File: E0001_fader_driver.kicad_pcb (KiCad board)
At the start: 4 copper layers, 107 x 17 mm, 53 parts, among them J1 SM04B-GHS-TB, J2 61300611021, U1 STM32C051F6P6, U2 MCP1703AT-3302E/MB, U3 DRV8210PDSGR, U4 TPS259470ARPW

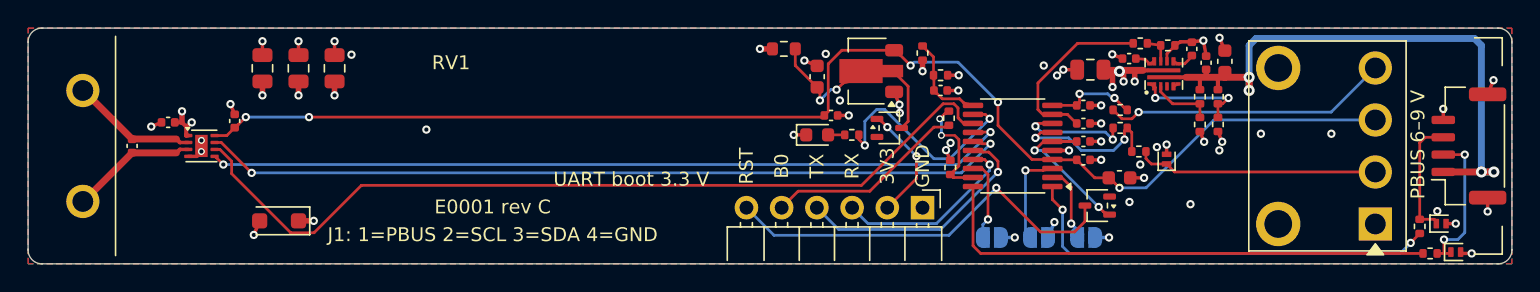
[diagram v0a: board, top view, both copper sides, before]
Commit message: TraceMaker experiment: placed (tracemaker-place routable, U3/U4/RV1 locked, hand intent fixes)
Tracks and vias stripped. RV1 locked. Placement from tracemaker-place
--mode routable on a proxy (RV1 courtyards as footprint keep-outs, F/B
pours removed), then C13, C1, C6, C7, C17 moved next to their IC pins
and silkscreen nudges. Not for fab.

Co-Authored-By: Claude Opus 5.5 <noreply@anthropic.com>
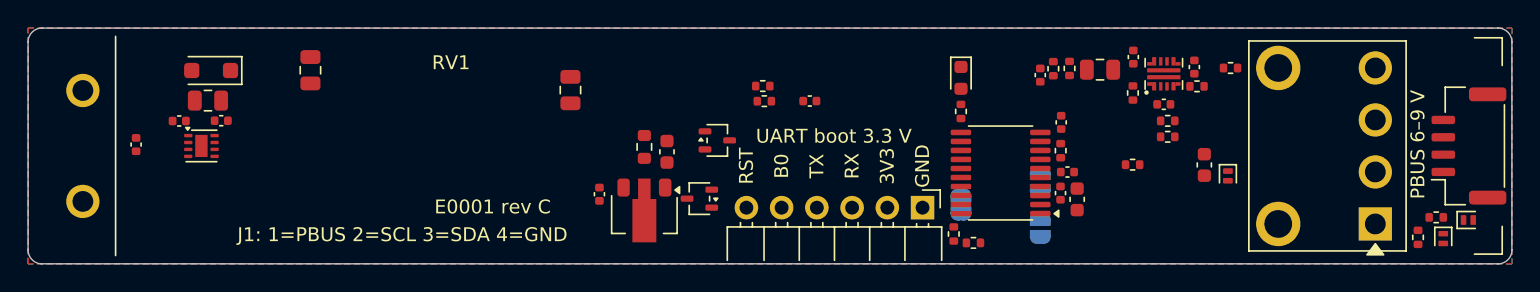
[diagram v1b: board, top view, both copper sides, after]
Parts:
- moved D6 27.8 mm to (116.2, 99.6), turned to 0 degrees
- moved C12 19.7 mm to (105.6, 96.0)
- moved U2 19.1 mm to (110.9, 105.0), turned to -90 degrees
- moved C3 17.6 mm to (107.7, 103.5), turned to -90 degrees
- moved D7 14.6 mm to (114.9, 103.8), turned to 180 degrees
- moved R9 12.8 mm to (119.6, 96.8), turned to 180 degrees
- moved R2 12.3 mm to (110.9, 100.1), turned to -90 degrees
- moved C2 12.1 mm to (112.6, 100.4)
- moved D1 11.9 mm to (79.7, 94.6)
- moved R8 11.8 mm to (119.5, 95.7), turned to 0 degrees
- moved D3 11.2 mm to (133.8, 95.1), turned to -90 degrees
- moved C9 9.46 mm to (122.9, 96.8), turned to 180 degrees
- moved C20 9.42 mm to (79.5, 96.7), turned to 180 degrees
- moved R7 8.51 mm to (153.2, 94.4), turned to 180 degrees
- moved R18 8.36 mm to (133.2, 106.3), turned to -90 degrees
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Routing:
- net +3V3: track 95.5 -> 0.00 mm, vias 5 -> 0
- net /MOT_IN1: track 62.6 -> 0.00 mm
- net /MOT_nSLEEP: track 59.0 -> 0.00 mm, vias 2 -> 0
- net /MOT_IN2: track 58.4 -> 0.00 mm, vias 2 -> 0
- net /PBUS_IN: track 42.7 -> 0.00 mm, vias 4 -> 0
- net /I2C_SCL: track 37.0 -> 0.00 mm
- net GND: track 34.9 -> 0.00 mm, vias 52 -> 0
- net /I2C_SDA: track 31.2 -> 0.00 mm, vias 2 -> 0
- net /J2_NRST: track 29.4 -> 0.00 mm, vias 1 -> 0
- net /FADER_WIPER: track 20.7 -> 0.00 mm, vias 1 -> 0
- net /UART_TX: track 18.3 -> 0.00 mm, vias 1 -> 0
- net /TOUCH_ELEC: track 17.4 -> 0.00 mm
- net /LED: track 16.0 -> 0.00 mm, vias 2 -> 0
- net /LDO_IN: track 15.1 -> 0.00 mm, vias 2 -> 0
- net VM_P: track 14.8 -> 0.00 mm, vias 12 -> 0
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
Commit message: TraceMaker experiment: routed (tm_route.sh pass 2)
eFuse support network (R11-R16, C15-C18, C1) moved back to its rev C
arrangement round U4, R7 moved for it: in pass 1 the placer's packing left
U4's bar pads no escape. Then tm_route.sh --fast-bends, TM_THREADS=1,
I2C/touch clearance rules in the routing dru: 73/73 routed, 211 tracks,
32 vias. DRC still has 5 unconnected (U4 split pads, one GND pocket) and
one hole_to_hole warning. Not for fab.

Co-Authored-By: Claude Opus 5.5 <noreply@anthropic.com>
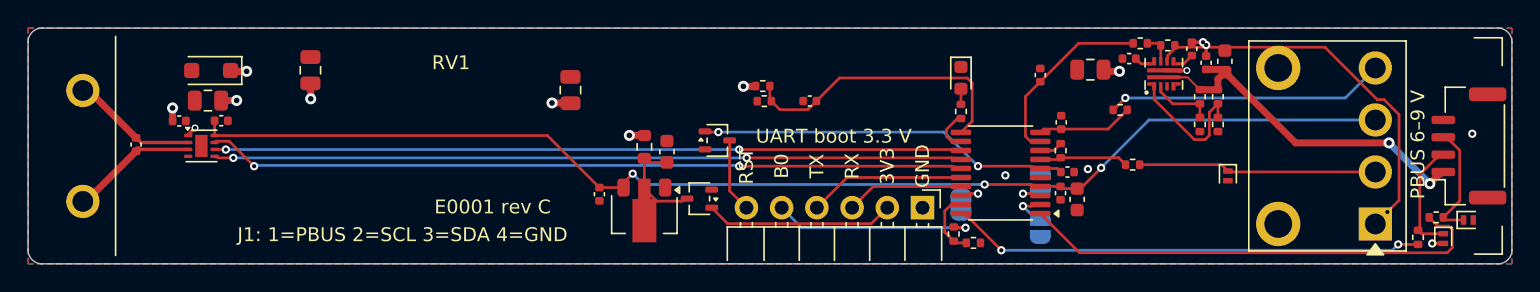
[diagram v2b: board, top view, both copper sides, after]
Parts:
- moved R7 8.51 mm to (145.2, 97.4), turned to 0 degrees
- moved C18 7.62 mm to (152.8, 93.9), turned to 90 degrees
- moved R15 7.28 mm to (148.7, 92.8), turned to 0 degrees
- moved R12 6.54 mm to (152.3, 98.5)
- moved R16 6.53 mm to (146.7, 92.6), turned to 180 degrees
- moved C17 4.28 mm to (151.4, 94.0), turned to 90 degrees
- moved R13 3.71 mm to (151.0, 96.5), turned to -90 degrees
- moved R14 2.33 mm to (151.0, 98.5), turned to -90 degrees
- moved R11 1.69 mm to (152.3, 96.5), turned to -90 degrees
- moved C16 1.32 mm to (150.4, 93.0), turned to 90 degrees
- moved C1 0.70 mm to (143.1, 94.5)
- moved C15 0.32 mm to (145.9, 93.7), turned to 180 degrees
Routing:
- net +3V3: track 0.00 -> 89.3 mm, vias 0 -> 3
- net /MOT_nSLEEP: track 0.00 -> 54.7 mm, vias 0 -> 2
- net /MOT_IN2: track 0.00 -> 53.8 mm, vias 0 -> 2
- net /MOT_IN1: track 0.00 -> 53.8 mm, vias 0 -> 2
- net /I2C_SDA: track 0.00 -> 34.4 mm
- net /I2C_SCL: track 0.00 -> 34.2 mm, vias 0 -> 2
- net GND: track 0.00 -> 29.1 mm, vias 0 -> 7
- net /NRST: track 0.00 -> 26.8 mm, vias 0 -> 2
- net /PBUS_IN: track 0.00 -> 26.6 mm, vias 0 -> 2
- net /VSENSE: track 0.00 -> 20.9 mm
- net /FADER_WIPER: track 0.00 -> 20.2 mm, vias 0 -> 1
- net /TOUCH_ELEC: track 0.00 -> 17.2 mm
- net /J2_BOOT0: track 0.00 -> 14.7 mm, vias 0 -> 1
- net /J2_3V3: track 0.00 -> 13.6 mm
- net /ILM_ADC: track 0.00 -> 13.4 mm
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
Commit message: TraceMaker experiment: DRC-clean, TRACEMAKER_LAYOUT.md
Hand fixes after tm_route.sh pass 2: U4 split-pad joins, VM_P/PBUS_IN
out of U4's bars at 0.5 mm with necks only in the pin field, motor loop
necks only at U3's pins, U3.1 to C13 direct, one GND pocket tied to In1,
the hole_to_hole via pair merged, acute and right-angle joins removed.
KiCad 10.0.6 DRC with parity: 0 errors / 0 unconnected / 0 parity, only
the known J2 lib_footprint_mismatch warning. tm_viapad, slots and corners
all 0. Report and comparison with rev C and the Freerouting re-route in
TRACEMAKER_LAYOUT.md. Not for fab.

Co-Authored-By: Claude Opus 5.5 <noreply@anthropic.com>
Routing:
- net VM_P: track 11.2 -> 13.8 mm, vias 10 -> 8
- net /PBUS_IN: track 26.6 -> 25.7 mm
- net /EF_EN: track 9.76 -> 9.15 mm
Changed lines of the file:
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@@
 	)
 	(segment
-		(start 148.4 94.55)
-		(end 149.58 94.56)
-		(width 0.3)
-		(layer "F.Cu")
-		(net "VM_P")
-	)
-	(segment
-		(start 78.06 99.18)
-		(end 78.54 98.7)
+		(start 146.82 94.68)
+		(end 145.26 94.68)
+		(width 0.5)
+		(layer "F.Cu")
+		(net "VM_P")
+	)
+	(segment
+		(start 78.05 99.25)
+		(end 77.7 99.25)
 		(width 0.25)
 		(layer "F.Cu")
@@
 	)
 	(segment
-		(start 149.58 94.56)
-		(end 150.06 94.56)
-		(width 0.3)
+		(start 145.26 94.68)
+		(end 145.2 94.62)
+		(width 0.5)
+		(layer "F.Cu")
+		(net "VM_P")
+	)
+	(segment
+		(start 77.35 98.9)
+		(end 76.92 98.47)
+		(width 0.5)
+		(layer "F.Cu")
+		(net "VM_P")
+	)
+	(segment
+		(start 146.95 94.55)
+		(end 146.82 94.68)
+		(width 0.25)
+		(layer "F.Cu")
+		(net "VM_P")
+	)
+	(segment
+		(start 76.92 98.47)
+		(end 76.92 98.2)
+		(width 0.5)
 		(layer "F.Cu")
 		(net "VM_P")
@@
 	)
 	(segment
+		(start 77.7 99.25)
+		(end 77.35 98.9)
+		(width 0.25)
+		(layer "F.Cu")
+		(net "VM_P")
+	)
+	(segment
 		(start 104.94 96.9)
 		(end 104.28 96.9)
@@
 	)
 	(segment
-		(start 78.05 99.25)
-		(end 78.06 99.18)
+		(start 148.4 94.55)
+		(end 146.95 94.55)
 		(width 0.25)
 		(layer "F.Cu")
@@
 	)
 	(via
-		(at 150.06 94.56)
-		(size 0.5)
-		(drill 0.3)
-		(layers "F.Cu" "B.Cu")
-		(net "VM_P")
-	)
-	(via
 		(at 81.54 96.72)
 		(size 0.8)
@@
 		(net "VM_P")
 	)
-	(via
-		(at 78.54 98.7)
-		(size 0.5)
-		(drill 0.3)
-		(layers "F.Cu" "B.Cu")
-		(net "VM_P")
-	)
 	(segment
 		(start 168.55 107.03)
@@
 	(segment
 		(start 151.45 93.52)
-		(end 151.45 92.72)
+		(end 151.22 92.52)
 		(width 0.25)
 		(layer "F.Cu")
@@
 	)
 	(via
+		(at 149.44 97.55)
+		(size 0.6)
+		(drill 0.3)
+		(layers "F.Cu" "B.Cu")
+		(net "GND")
+	)
+	(via
 		(at 170.64 99.12)
 		(size 0.6)
@@
 	(via
 		(at 167.75 107.03)
-		(size 0.6)
-		(drill 0.3)
-		(layers "F.Cu" "B.Cu")
-		(net "GND")
-	)
-	(via
-		(at 151.45 92.72)
 		(size 0.6)
 		(drill 0.3)
@@
 	)
 	(segment
+		(start 147.375 94.075)
+		(end 147.703 93.9)
+		(width 0.2)
+		(layer "F.Cu")
+		(net "/EF_ITIMER")
+	)
+	(segment
 		(start 146.38 93.7)
 		(end 146.755 94.075)
@@
 	)
 	(segment
-		(start 152.8 94.675)
+		(start 152.55 94.925)
 		(end 152.3 95.175)
 		(width 0.5)
-		(layer "F.Cu")
-		(net "/PBUS_IN")
-	)
-	(segment
-		(start 150.11 95.05)
-		(end 148.4 95.05)
-		(width 0.168)
 		(layer "F.Cu")
 		(net "/PBUS_IN")
@@
 	)
 	(segment
-		(start 152.8 94.675)
-		(end 152.605 94.48)
-		(width 0.5)
+		(start 148.4 95.05)
+		(end 149.85 95.05)
+		(width 0.25)
 		(layer "F.Cu")
 		(net "/PBUS_IN")
@@
 	)
 	(segment
+		(start 150.11 95.05)
+		(end 151 95.94)
+		(width 0.5)
+		(layer "F.Cu")
+		(net "/PBUS_IN")
+	)
+	(segment
 		(start 157.905 99.78)
 		(end 152.8 94.675)
@@
 	)
 	(segment
-		(start 152.3 95.94)
+		(start 149.85 95.05)
+		(end 150.11 95.05)
+		(width 0.5)
+		(layer "F.Cu")
+		(net "/PBUS_IN")
+	)
+	(segment
+		(start 152.1 95.94)
 		(end 151 95.94)
 		(width 0.5)
@@
 		(end 151.45 94.48)
 		(width 0.5)
-		(layer "F.Cu")
-		(net "/PBUS_IN")
-	)
-	(segment
-		(start 151 95.94)
-		(end 150.11 95.05)
-		(width 0.15)
 		(layer "F.Cu")
 		(net "/PBUS_IN")
@@
 	)
 	(segment
-		(start 168.74 105.34)
+		(start 168.7 105.34)
 		(end 170.01 105.34)
-		(width 0.2)
-		(layer "F.Cu")
-		(net "/J1_SDA")
-	)
-	(segment
-		(start 168.55 105.15)
-		(end 168.74 105.34)
 		(width 0.2)
 		(layer "F.Cu")
@@
 	(segment
 		(start 103.95 99.25)
-		(end 79.95 99.25)
+		(end 80.15 99.25)
 		(width 0.2)
 		(layer "F.Cu")
@@
 	)
 	(segment
+		(start 149.425 94.075)
+		(end 149.097 93.9)
+		(width 0.2)
+		(layer "F.Cu")
+		(net "/EF_DVDT")
+	)
+	(segment
 		(start 153.02 101.81)
 		(end 153.085 101.875)
@@
 	(segment
 		(start 147.703 95.7)
+		(end 147.375 95.525)
+		(width 0.2)
+		(layer "F.Cu")
+		(net "/EF_EN")
+	)
+	(segment
+		(start 147.703 95.7)
 		(end 147.703 96.643)
 		(width 0.2)
@@
 	(segment
 		(start 151.68 99.24)
-		(end 151.68 97.58)
-		(width 0.2)
-		(layer "F.Cu")
-		(net "/EF_EN")
-	)
-	(segment
-		(start 151.68 97.58)
-		(end 152.3 96.96)
+		(end 151.68 98.56)
 		(width 0.2)
 		(layer "F.Cu")
@@
 	)
 	(segment
+		(start 151.68 98.56)
+		(end 152.3 97.94)
+		(width 0.2)
+		(layer "F.Cu")
+		(net "/EF_EN")
+	)
+	(segment
 		(start 152.3 96.96)
 		(end 152.3 97.94)
@@
 	(segment
 		(start 149.04 96.96)
-		(end 151 96.96)
+		(end 150.82 96.96)
 		(width 0.2)
 		(layer "F.Cu")
@@
 	)
 	(segment
+		(start 149.097 95.7)
+		(end 149.425 95.525)
+		(width 0.2)
+		(layer "F.Cu")
+		(net "unconnected-(U4-~{FLT}-Pad4)")
+	)
+	(segment
 		(start 148.175 93.9)
 		(end 148.175 92.75)
@@
 	)
 	(segment
-		(start 110.94 100.895)
-		(end 111.24 101.195)
-		(width 0.2)
-		(layer "F.Cu")
-		(net "/LDO_IN")
-	)
-	(segment
 		(start 110.94 103.0875)
 		(end 110.94 100.895)
@@
 	)
 	(segment
-		(start 111.24 101.195)
+		(start 111 101.195)
 		(end 112.57 101.195)
 		(width 0.2)
@@
 	)
 	(segment
-		(start 74.42 100.25)
-		(end 78.05 100.25)
+		(start 77.6 100.25)
+		(end 77.4 100.45)
 		(width 0.25)
 		(layer "F.Cu")
@@
 	)
 	(segment
-		(start 74.29 100.38)
-		(end 74.42 100.25)
+		(start 77.4 100.45)
+		(end 74.29 100.45)
 		(width 0.5)
 		(layer "F.Cu")
 		(net "/MOTOR_P")
+	)
+	(segment
+		(start 78.05 100.25)
+		(end 77.6 100.25)
+		(width 0.25)
+		(layer "F.Cu")
+		(net "/MOTOR_P")
+	)
+	(segment
+		(start 77.3 99.75)
+		(end 77.15 99.6)
+		(width 0.25)
+		(layer "F.Cu")
+		(net "/MOTOR_N")
+	)
+	(segment
+		(start 77.15 99.6)
+		(end 74.29 99.6)
+		(width 0.5)
+		(layer "F.Cu")
+		(net "/MOTOR_N")
 	)
 	(segment
@@
 	)
 	(segment
-		(start 74.29 99.42)
-		(end 74.62 99.75)
-		(width 0.237)
-		(layer "F.Cu")
-		(net "/MOTOR_N")
-	)
-	(segment
 		(start 70.87 96)
 		(end 70.45 96)
@@
 	)
 	(segment
-		(start 74.62 99.75)
-		(end 78.05 99.75)
+		(start 78.05 99.75)
+		(end 77.3 99.75)
 		(width 0.25)
 		(layer "F.Cu")

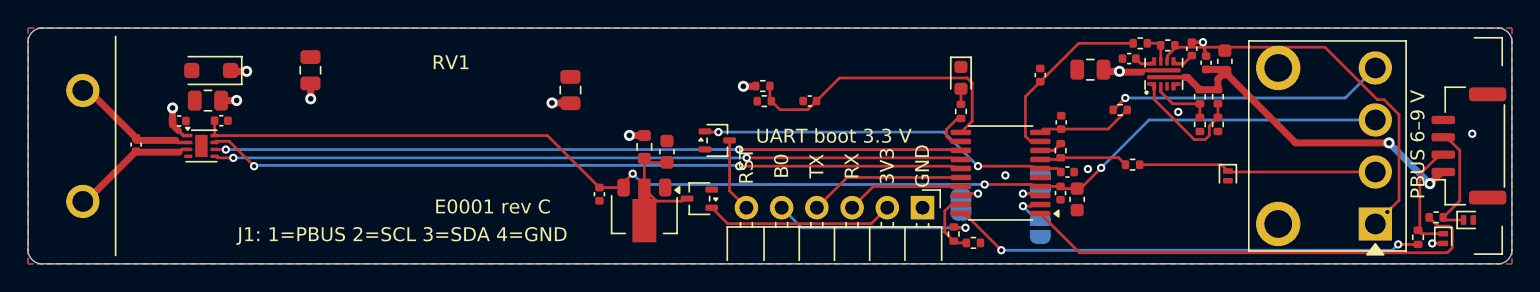
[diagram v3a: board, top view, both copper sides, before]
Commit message: TraceMaker round 2: stripped, C9/C19 back at U1, GND fan-out, I2C rule in dru
Tracks and vias stripped (placement kept). C9, R8, R9 next to U1.11,
C7 and C19 next to U1.10/U1.9, R6 moved east to free U1.9. Every
capacitor GND pad gets its own locked 0.6/0.3 via to In1 (18), at a
multiple of 45 deg and >= 0.15 mm from every pad. I2C >= 1.85 mm from
the touch electrode (and >= 0.5 mm from TOUCH_SNS/DRV) now in the
project dru. Not for fab.

Co-Authored-By: Claude Opus 5.5 <noreply@anthropic.com>
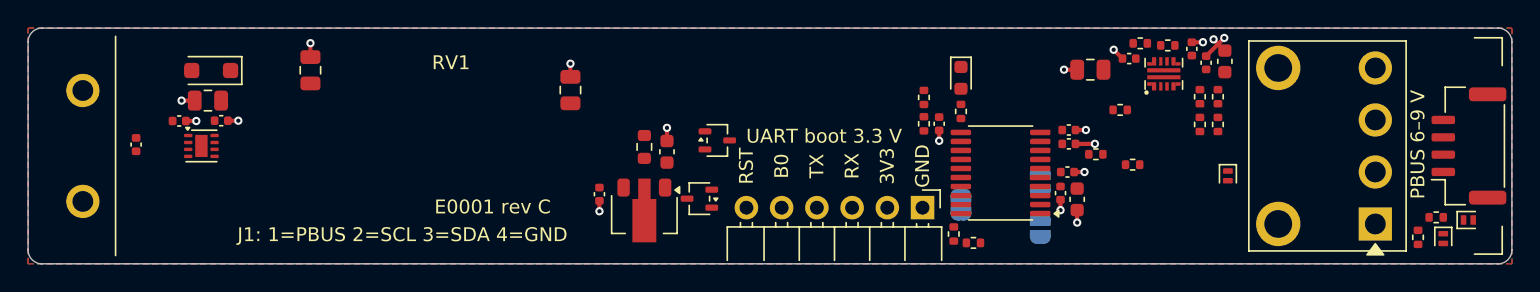
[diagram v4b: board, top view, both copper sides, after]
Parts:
- moved R8 11.6 mm to (131.1, 96.5), turned to -90 degrees
- moved R9 11.6 mm to (131.1, 98.4), turned to -90 degrees
- moved C9 9.47 mm to (132.2, 98.4), turned to -90 degrees
- moved C19 5.37 mm to (141.6, 99.8), turned to 0 degrees
- moved R6 2.55 mm to (143.5, 100.6), turned to 0 degrees
- moved C7 0.78 mm to (141.6, 98.8), turned to 0 degrees
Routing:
- net +3V3: track 89.1 -> 0.00 mm, vias 3 -> 0
- net /MOT_nSLEEP: track 54.7 -> 0.00 mm, vias 2 -> 0
- net /MOT_IN2: track 53.8 -> 0.00 mm, vias 2 -> 0
- net /MOT_IN1: track 53.8 -> 0.00 mm, vias 2 -> 0
- net /I2C_SDA: track 34.4 -> 0.00 mm
- net /I2C_SCL: track 34.2 -> 0.00 mm, vias 2 -> 0
- net /NRST: track 26.8 -> 0.00 mm, vias 2 -> 0
- net /PBUS_IN: track 25.7 -> 0.00 mm, vias 2 -> 0
- net /VSENSE: track 20.9 -> 0.00 mm
- net /FADER_WIPER: track 20.2 -> 0.00 mm, vias 1 -> 0
- net /TOUCH_ELEC: track 17.2 -> 0.00 mm
- net /J2_BOOT0: track 14.7 -> 0.00 mm, vias 1 -> 0
- net VM_P: track 13.8 -> 0.00 mm, vias 8 -> 0
- net /J2_3V3: track 13.6 -> 0.00 mm
- net /ILM_ADC: track 13.4 -> 0.00 mm
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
